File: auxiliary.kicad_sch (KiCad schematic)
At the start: 69 parts, among them IC1 MAX1708EEE+, J4 BM04B-SRSS-TB-LF-SN, J5 SM06B-SRSS-TB(LF)(SN), J6 SM09B-SRSS-TB(LF)(SN), Q1 BSS138AKA, U1 PCA9547BS,118, U2 NTS0102DP

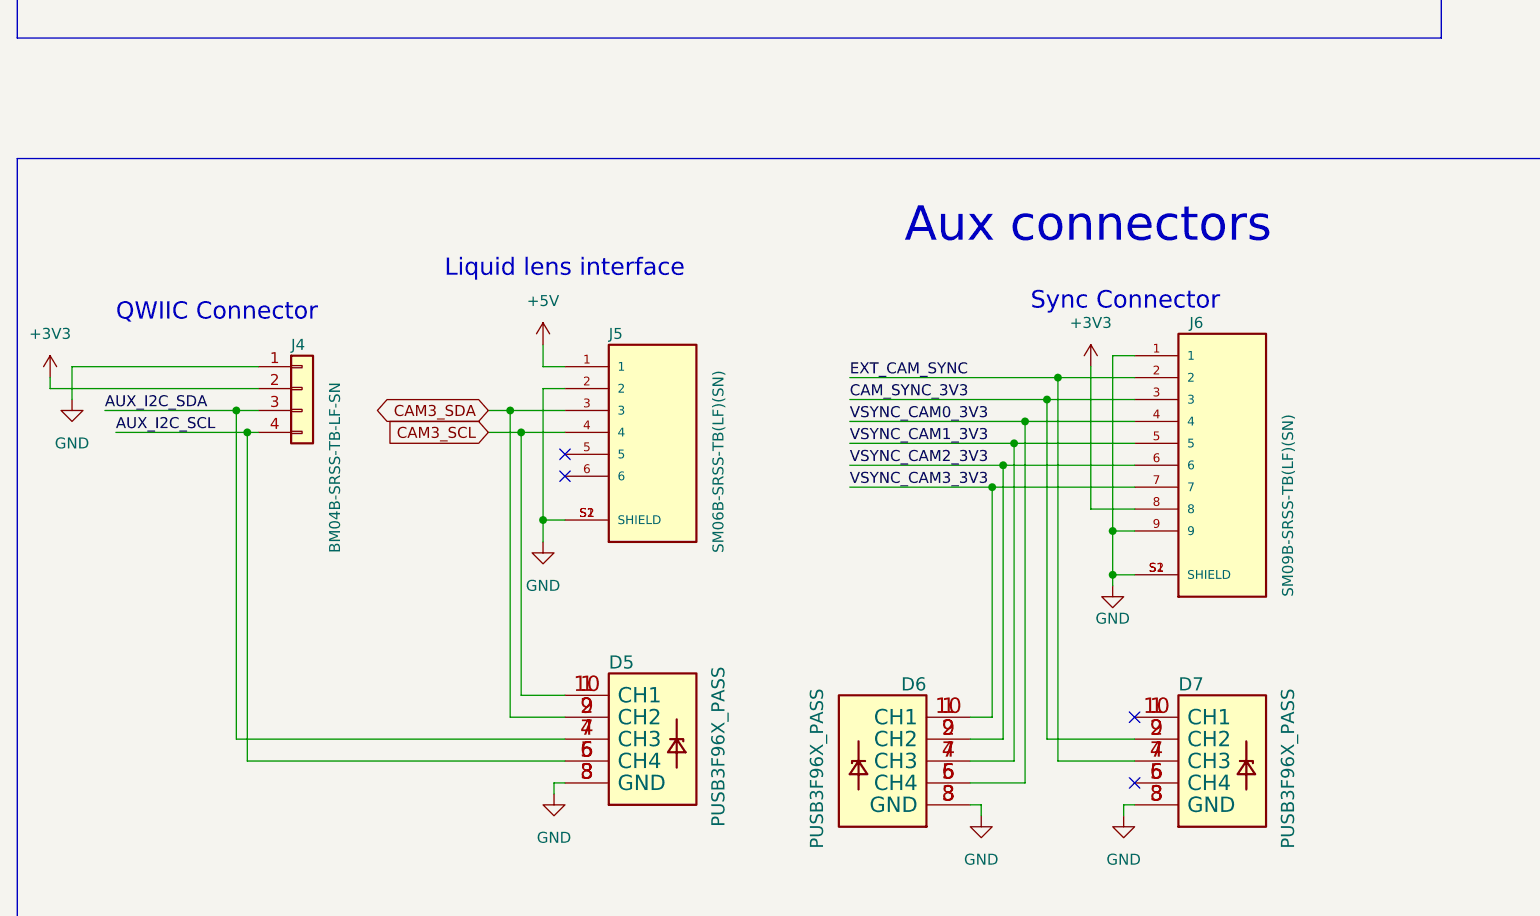
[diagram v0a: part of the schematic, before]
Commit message: Added fuses for aux connectors
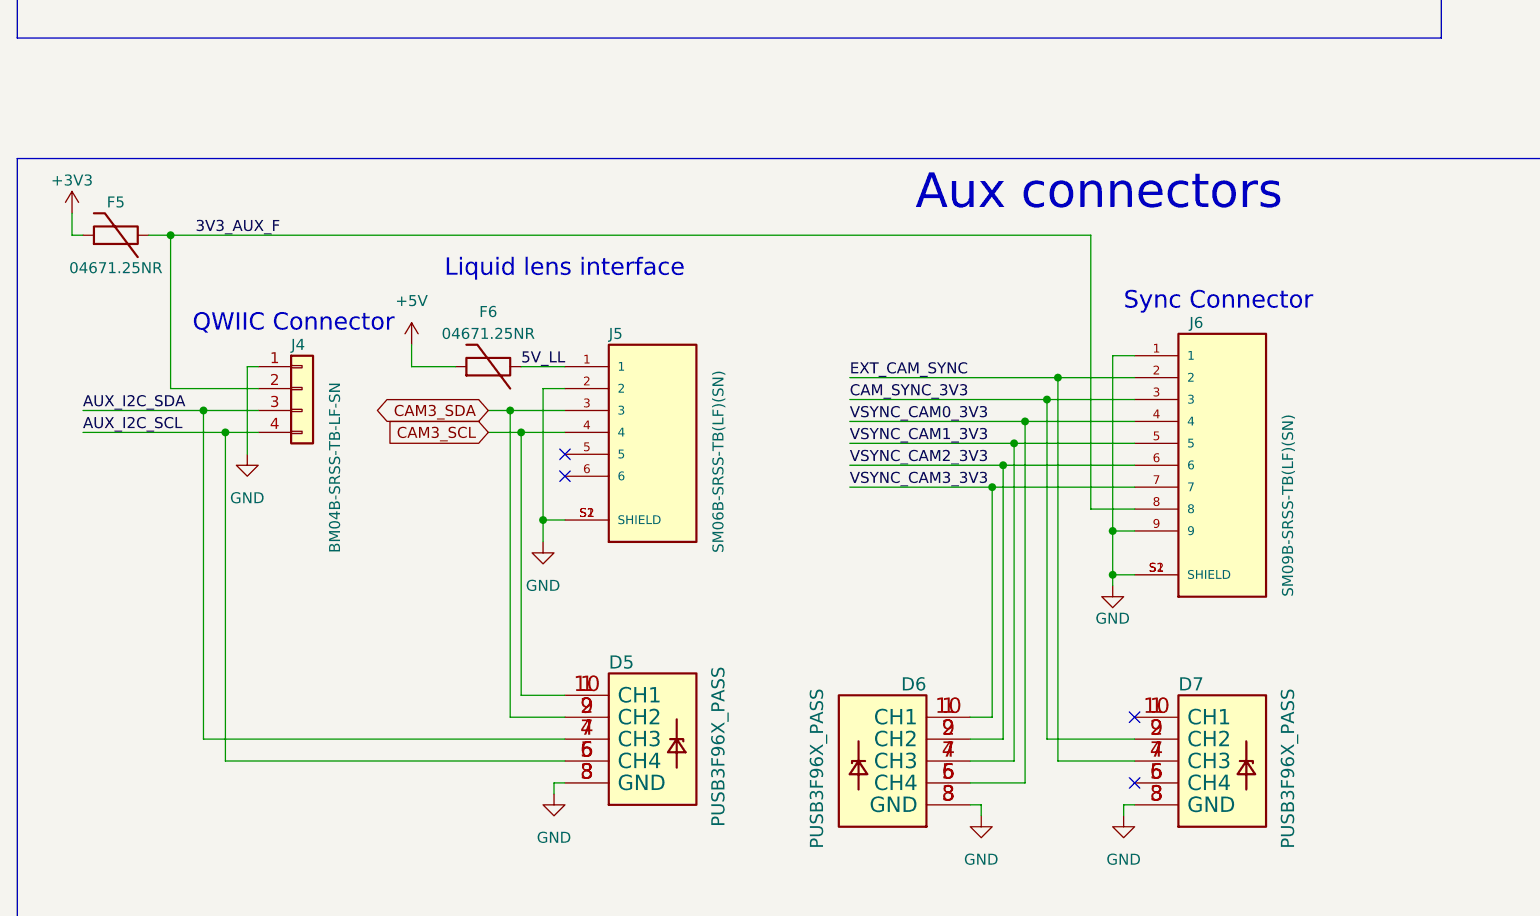
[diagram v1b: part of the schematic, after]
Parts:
- added F5, F6: 04671.25NR, antmicro-footprints:0603-Fuse-Littelfuse-0467, symbol antmicroFuses:04671.25NR
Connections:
- net +3V3: now also F5.2; no longer J4.2 (Pin_2), J6.8
- net +5V: now also F6.2; no longer J5.1
- new net 3V3_AUX_F: F5.1, J4.2 (Pin_2), J6.8
- new net 5V_LL: F6.1, J5.1

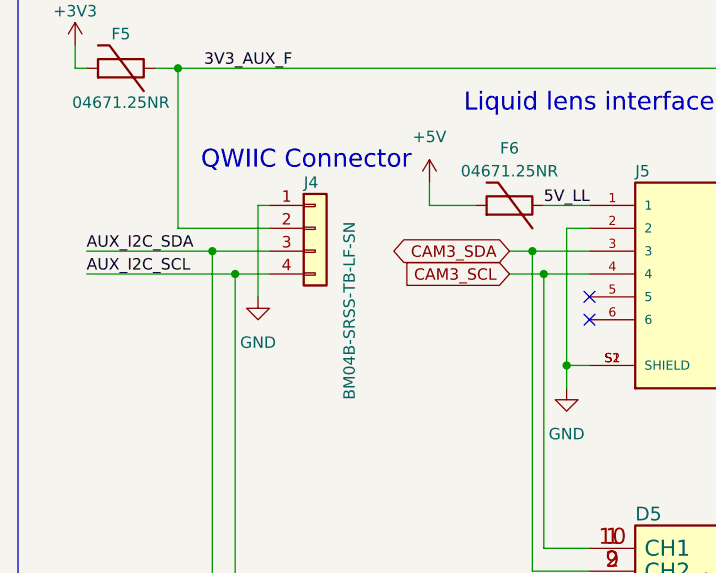
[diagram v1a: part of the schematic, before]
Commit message: Swapped QWIIC connector to a side entry one
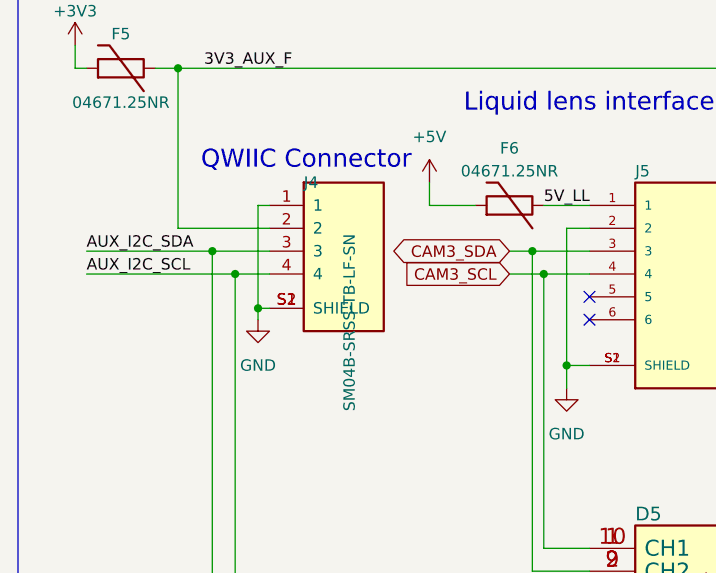
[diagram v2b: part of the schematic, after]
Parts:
- removed J4: BM04B-SRSS-TB-LF-SN, antmicro-footprints:BM04B-SRSS-TB-LF-SN, symbol antmicroRectangularConnectorsHeadersMalePins:BM04B-SRSS-TB-LF-SN
- added J4: SM04B-SRSS-TB-LF-SN, antmicro-footprints:SM04B-SRSS-TB-LF-SN, symbol antmicroRectangularConnectorsHeadersMalePins:SM04B-SRSS-TB-LF-SN
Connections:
- net 3V3_AUX_F: now also J4.2
- net AUX_I2C_SCL: now also J4.4
- net AUX_I2C_SDA: now also J4.3
- net GND: now also J4.1, J4.S1 (SHIELD), J4.S2 (SHIELD)
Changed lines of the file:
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@@
   (junction (at 351.79 175.26) (diameter 0) (color 0 0 0 0)
   )
+  (junction (at 52.07 191.77) (diameter 0) (color 0 0 0 0)
+  )
   (junction (at 351.79 167.64) (diameter 0) (color 0 0 0 0)
   )
@@
     (stroke (width 0) (type default) (color 0 0 0 0))
   )
+  (wire (pts (xy 52.07 191.77) (xy 53.34 191.77))
+    (stroke (width 0) (type default) (color 0 0 0 0))
+  )
   (wire (pts (xy 313.69 152.4) (xy 314.96 152.4))
     (stroke (width 0) (type default) (color 0 0 0 0))
@@
     (stroke (width 0) (type default) (color 0 0 0 0))
   )
-  (wire (pts (xy 52.07 190.5) (xy 52.07 180.34))
+  (wire (pts (xy 52.07 193.04) (xy 52.07 191.77))
     (stroke (width 0) (type default) (color 0 0 0 0))
   )
@@
     (stroke (width 0) (type default) (color 0 0 0 0))
   )
+  (wire (pts (xy 52.07 191.77) (xy 52.07 180.34))
+    (stroke (width 0) (type default) (color 0 0 0 0))
+  )
   (wire (pts (xy 337.82 134.62) (xy 351.79 134.62))
     (stroke (width 0) (type default) (color 0 0 0 0))
@@
     (pin "1")
   )
-  (symbol (lib_id "antmicroRectangularConnectorsHeadersMalePins:BM04B-SRSS-TB-LF-SN") (at 58.42 186.69 0) (unit 1)
-    (in_bom yes) (on_board yes)
-    (property "Reference" "J4" (id 0) (at 57.15 177.8 0)
-      (effects (font (size 1.27 1.27)) (justify left))
-    )
-    (property "Value" "BM04B-SRSS-TB-LF-SN" (id 1) (at 62.23 201.93 90)
-      (effects (font (size 1.27 1.27)) (justify left))
-    )
-    (property "Footprint" "antmicro-footprints:BM04B-SRSS-TB-LF-SN" (id 2) (at 58.42 193.04 0)
-      (effects (font (size 1.27 1.27)) hide)
-    )
-    (property "Datasheet" "https://www.jst-mfg.com/product/pdf/eng/eSH.pdf" (id 3) (at 46.99 194.31 0)
-      (effects (font (size 1.27 1.27)) hide)
-    )
-    (property "MPN" "BM04B-SRSS-TB(LF)(SN) " (id 4) (at 55.88 195.58 0)
-      (effects (font (size 1.27 1.27)) (justify left) hide)
-    )
-    (property "Manufacturer" "JST" (id 5) (at 55.88 198.12 0)
-      (effects (font (size 1.27 1.27)) (justify left) hide)
-    )
-    (pin "1")
-    (pin "2")
-    (pin "3")
-    (pin "4")
-  )
   (symbol (lib_id "antmicroTestPoints:TP_SMD_0_75MM") (at 111.76 46.99 180) (unit 1)
     (in_bom yes) (on_board yes)
@@
     (pin "2")
   )
+  (symbol (lib_id "antmicroRectangularConnectorsHeadersMalePins:SM04B-SRSS-TB-LF-SN") (at 58.42 186.69 0) (unit 1)
+    (in_bom yes) (on_board yes)
+    (property "Reference" "J4" (id 0) (at 57.15 177.8 0)
+      (effects (font (size 1.27 1.27)) (justify left))
+    )
+    (property "Value" "SM04B-SRSS-TB-LF-SN" (id 1) (at 62.23 203.2 90)
+      (effects (font (size 1.27 1.27)) (justify left))
+    )
+    (property "Footprint" "antmicro-footprints:SM04B-SRSS-TB-LF-SN" (id 2) (at 58.42 193.04 0)
+      (effects (font (size 1.27 1.27)) hide)
+    )
+    (property "Datasheet" "https://www.jst-mfg.com/product/pdf/eng/eSH.pdf" (id 3) (at 46.99 194.31 0)
+      (effects (font (size 1.27 1.27)) hide)
+    )
+    (property "MPN" "SM04B-SRSS-TB-LF-SN" (id 4) (at 55.88 195.58 0)
+      (effects (font (size 1.27 1.27)) (justify left) hide)
+    )
+    (property "Manufacturer" "JST" (id 5) (at 55.88 198.12 0)
+      (effects (font (size 1.27 1.27)) (justify left) hide)
+    )
+    (pin "1")
+    (pin "2")
+    (pin "3")
+    (pin "4")
+    (pin "S1")
+    (pin "S2")
+  )
   (symbol (lib_id "antmicroResistors0402:R_2k_0402") (at 158.75 81.28 90) (unit 1)
     (in_bom yes) (on_board yes)
@@
     (pin "2")
   )
-  (symbol (lib_id "power:GND") (at 52.07 190.5 0) (unit 1)
+  (symbol (lib_id "power:GND") (at 52.07 193.04 0) (unit 1)
     (in_bom yes) (on_board yes) (fields_autoplaced)
-    (property "Reference" "#PWR01" (id 0) (at 52.07 196.85 0)
+    (property "Reference" "#PWR01" (id 0) (at 52.07 199.39 0)
       (effects (font (size 1.27 1.27)) hide)
     )
-    (property "Value" "GND" (id 1) (at 52.07 195.58 0))
-    (property "Footprint" "" (id 2) (at 52.07 190.5 0)
+    (property "Value" "GND" (id 1) (at 52.07 198.12 0))
+    (property "Footprint" "" (id 2) (at 52.07 193.04 0)
       (effects (font (size 1.27 1.27)) hide)
     )
-    (property "Datasheet" "" (id 3) (at 52.07 190.5 0)
+    (property "Datasheet" "" (id 3) (at 52.07 193.04 0)
       (effects (font (size 1.27 1.27)) hide)
     )

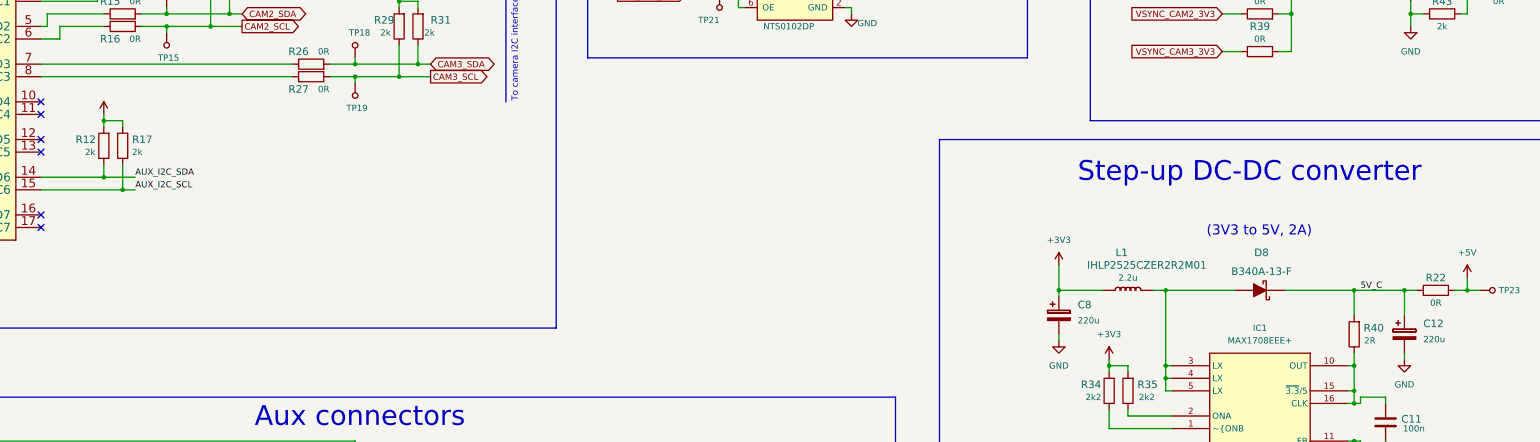
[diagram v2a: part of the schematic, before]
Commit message: Changed 5V converter capacitors to ceramic for lower ESR
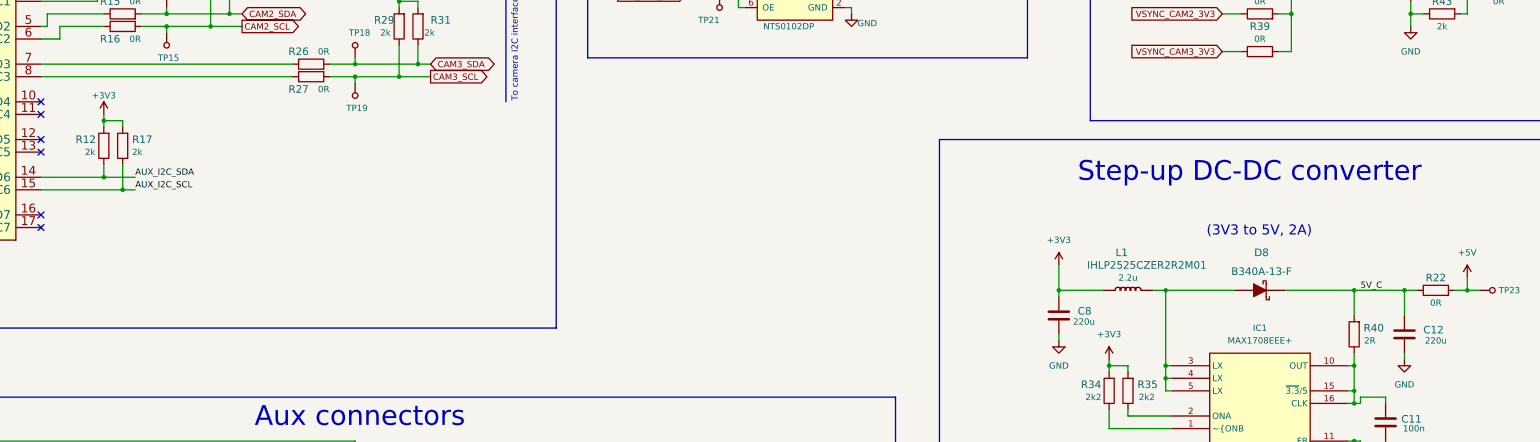
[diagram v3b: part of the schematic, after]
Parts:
- C12, C8: footprint antmicro-footprints:KEMET_D -> antmicro-footprints:1206-cap; symbol antmicroCapacitorspol:C_220u_KEMET_D -> antmicroCapacitorsmisc:C_220u_1206_6V3; MPN T491D227K016AT -> GRM31CR60J227ME11L; Manufacturer KEMET -> Murata
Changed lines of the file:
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@@
-    (pin "1")
-  )
-  (symbol (lib_id "power:+3V3") (at 99.06 99.06 0) (unit 1)
-    (in_bom yes) (on_board yes)
-    (property "Reference" "#PWR0132" (id 0) (at 99.06 102.87 0)
-      (effects (font (size 1.27 1.27)) hide)
-    )
-    (property "Value" "~" (id 1) (at 102.87 97.79 0))
-    (property "Footprint" "" (id 2) (at 99.06 99.06 0)
-      (effects (font (size 1.27 1.27)) hide)
-    )
-    (property "Datasheet" "" (id 3) (at 99.06 99.06 0)
-      (effects (font (size 1.27 1.27)) hide)
-    )
     (pin "1")
   )
@@
     (pin "2")
   )
-  (symbol (lib_id "antmicroCapacitorspol:C_220u_KEMET_D") (at 292.1 138.43 0) (unit 1)
-    (in_bom yes) (on_board yes) (fields_autoplaced)
-    (property "Reference" "C8" (id 0) (at 295.91 137.541 0)
-      (effects (font (size 1.524 1.524)) (justify left))
-    )
-    (property "Value" "C_220u_KEMET_D" (id 1) (at 292.1 142.24 0)
-      (effects (font (size 1.524 1.524)) hide)
-    )
-    (property "Footprint" "antmicro-footprints:KEMET_D" (id 2) (at 297.18 133.35 0)
-      (effects (font (size 1.524 1.524)) (justify left) hide)
-    )
-    (property "Datasheet" "" (id 3) (at 292.1 138.43 0)
-      (effects (font (size 1.27 1.27)) hide)
-    )
-    (property "Manufacturer" "KEMET" (id 4) (at 297.18 128.27 0)
-      (effects (font (size 1.524 1.524)) (justify left) hide)
-    )
-    (property "MPN" "T491D227K016AT" (id 5) (at 297.18 130.81 0)
-      (effects (font (size 1.524 1.524)) (justify left) hide)
-    )
-    (property "Val" "220u" (id 6) (at 295.91 140.7159 0)
-      (effects (font (size 1.27 1.27)) (justify left))
-    )
+  (symbol (lib_id "antmicroCapacitorsmisc:C_220u_1206_6V3") (at 292.1 139.7 0) (unit 1)
+    (in_bom yes) (on_board yes)
+    (property "Reference" "C8" (id 0) (at 295.91 138.811 0)
+      (effects (font (size 1.524 1.524)) (justify left))
+    )
+    (property "Value" "C_220u_KEMET_D" (id 1) (at 292.1 143.51 0)
+      (effects (font (size 1.524 1.524)) hide)
+    )
+    (property "Footprint" "antmicro-footprints:1206-cap" (id 2) (at 297.18 134.62 0)
+      (effects (font (size 1.524 1.524)) (justify left) hide)
+    )
+    (property "Datasheet" "" (id 3) (at 292.1 139.7 0)
+      (effects (font (size 1.27 1.27)) hide)
+    )
+    (property "Manufacturer" "Murata" (id 4) (at 297.18 129.54 0)
+      (effects (font (size 1.524 1.524)) (justify left) hide)
+    )
+    (property "MPN" "GRM31CR60J227ME11L" (id 5) (at 297.18 132.08 0)
+      (effects (font (size 1.524 1.524)) (justify left) hide)
+    )
+    (property "Val" "220u" (id 6) (at 297.18 140.97 0))
     (pin "1")
     (pin "2")
@@
     (pin "1")
   )
-  (symbol (lib_id "antmicroCapacitorspol:C_220u_KEMET_D") (at 361.95 142.24 0) (unit 1)
-    (in_bom yes) (on_board yes) (fields_autoplaced)
-    (property "Reference" "C12" (id 0) (at 365.76 141.351 0)
-      (effects (font (size 1.524 1.524)) (justify left))
-    )
-    (property "Value" "C_220u_KEMET_D" (id 1) (at 361.95 146.05 0)
-      (effects (font (size 1.524 1.524)) hide)
-    )
-    (property "Footprint" "antmicro-footprints:KEMET_D" (id 2) (at 367.03 137.16 0)
-      (effects (font (size 1.524 1.524)) (justify left) hide)
-    )
-    (property "Datasheet" "" (id 3) (at 361.95 142.24 0)
-      (effects (font (size 1.27 1.27)) hide)
-    )
-    (property "Manufacturer" "KEMET" (id 4) (at 367.03 132.08 0)
-      (effects (font (size 1.524 1.524)) (justify left) hide)
-    )
-    (property "MPN" "T491D227K016AT" (id 5) (at 367.03 134.62 0)
-      (effects (font (size 1.524 1.524)) (justify left) hide)
-    )
-    (property "Val" "220u" (id 6) (at 365.76 144.5259 0)
-      (effects (font (size 1.27 1.27)) (justify left))
-    )
-    (pin "1")
-    (pin "2")
+  (symbol (lib_id "power:+3V3") (at 99.06 99.06 0) (unit 1)
+    (in_bom yes) (on_board yes)
+    (property "Reference" "#PWR?" (id 0) (at 99.06 102.87 0)
+      (effects (font (size 1.27 1.27)) hide)
+    )
+    (property "Value" "+3V3" (id 1) (at 99.06 95.25 0))
+    (property "Footprint" "" (id 2) (at 99.06 99.06 0)
+      (effects (font (size 1.27 1.27)) hide)
+    )
+    (property "Datasheet" "" (id 3) (at 99.06 99.06 0)
+      (effects (font (size 1.27 1.27)) hide)
+    )
+    (pin "1")
+  )
+  (symbol (lib_id "antmicroCapacitorsmisc:C_220u_1206_6V3") (at 361.95 143.51 0) (unit 1)
+    (in_bom yes) (on_board yes)
+    (property "Reference" "C12" (id 0) (at 365.76 142.621 0)
+      (effects (font (size 1.524 1.524)) (justify left))
+    )
+    (property "Value" "C_220u_KEMET_D" (id 1) (at 361.95 147.32 0)
+      (effects (font (size 1.524 1.524)) hide)
+    )
+    (property "Footprint" "antmicro-footprints:1206-cap" (id 2) (at 367.03 138.43 0)
+      (effects (font (size 1.524 1.524)) (justify left) hide)
+    )
+    (property "Datasheet" "" (id 3) (at 361.95 143.51 0)
+      (effects (font (size 1.27 1.27)) hide)
+    )
+    (property "Manufacturer" "Murata" (id 4) (at 367.03 133.35 0)
+      (effects (font (size 1.524 1.524)) (justify left) hide)
+    )
+    (property "MPN" "GRM31CR60J227ME11L" (id 5) (at 367.03 135.89 0)
+      (effects (font (size 1.524 1.524)) (justify left) hide)
+    )
+    (property "Val" "220u" (id 6) (at 368.3 144.78 0))
+    (pin "1")
+    (pin "2")
